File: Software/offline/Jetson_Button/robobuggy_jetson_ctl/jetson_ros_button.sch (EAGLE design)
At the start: 4 parts, among them J1 22-27-2061-06

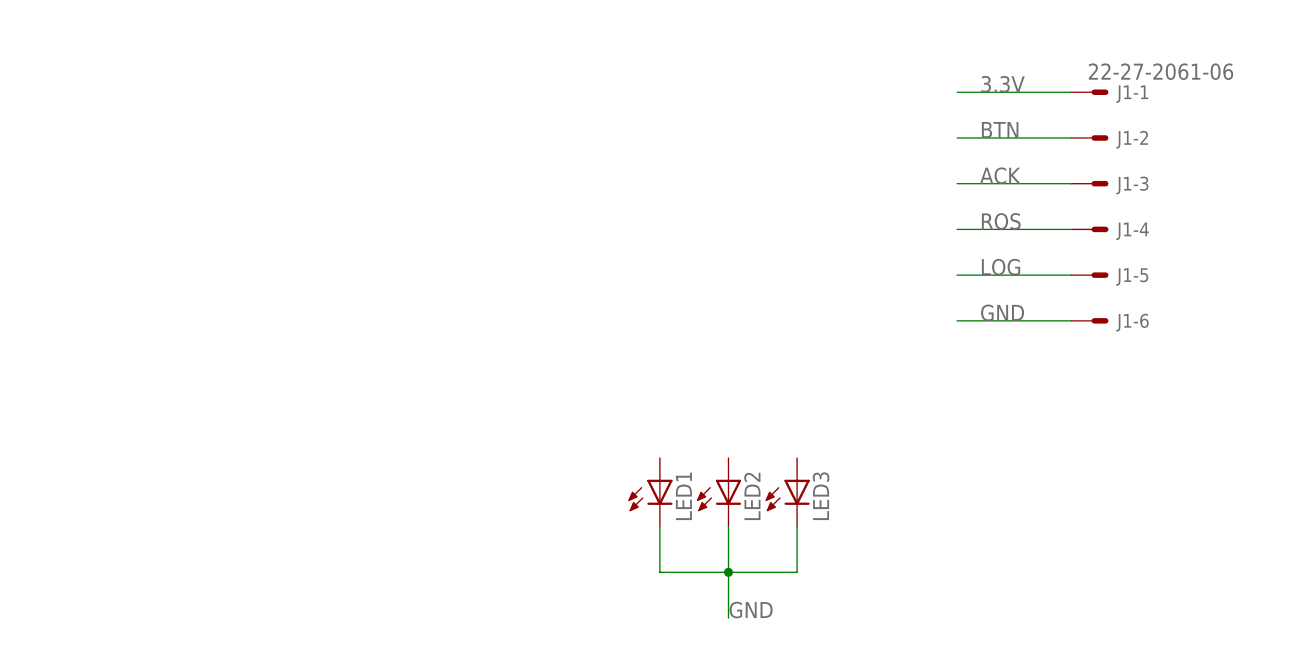
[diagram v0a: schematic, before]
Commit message: Changed connector so that it matches what is on the LED board
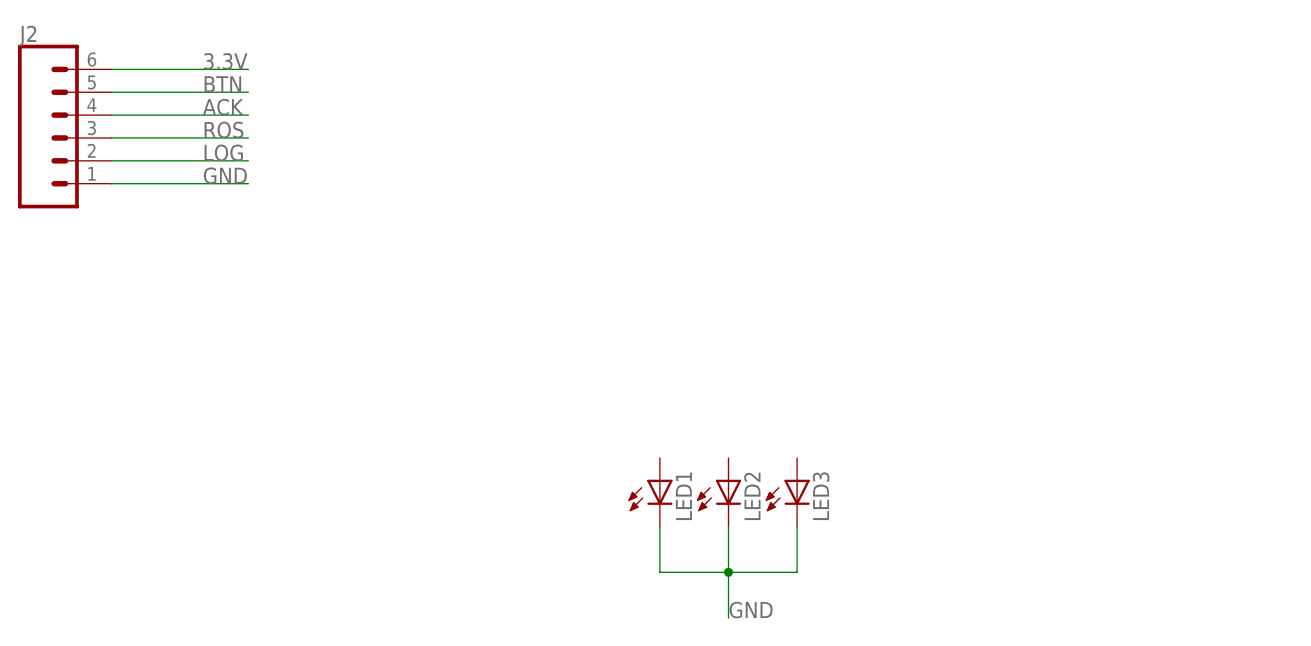
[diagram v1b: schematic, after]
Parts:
- removed J1: 22-27-2061-06, con-molex:22-27-2061-06
- added J2: (no value), SparkFun-Connectors:CONN_06SILK_FEMALE_PTH
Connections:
- net 3.3V: now also J2.6; no longer J1-1.S
- net ACK: now also J2.4; no longer J1-3.S
- net BTN: now also J2.5; no longer J1-2.S
- net GND: now also J2.1; no longer J1-6.S
- net LOG: now also J2.2; no longer J1-5.S
- net ROS: now also J2.3; no longer J1-4.S

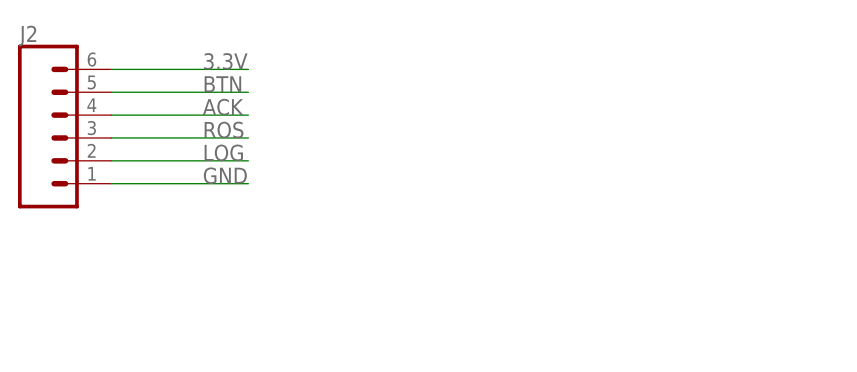
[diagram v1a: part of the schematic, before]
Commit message: Add the push button to the PCB
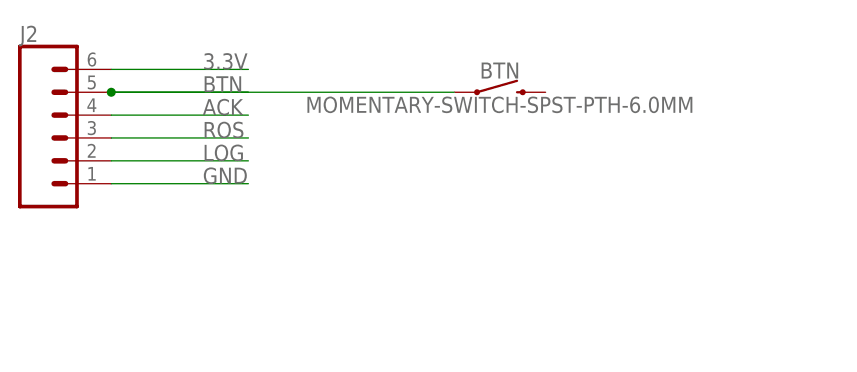
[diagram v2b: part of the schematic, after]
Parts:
- added BTN: MOMENTARY-SWITCH-SPST-PTH-6.0MM, SparkFun-Switches:MOMENTARY-SWITCH-SPST-PTH-6.0MM
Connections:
- net BTN: now also BTN.1
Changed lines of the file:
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@@
 <part name="LED3" library="eagle-ltspice" library_urn="urn:adsk.eagle:library:217" deviceset="LED_E" device="" package3d_urn="urn:adsk.eagle:package:13319/1"/>
 <part name="J2" library="SparkFun-Connectors" library_urn="urn:adsk.eagle:library:513" deviceset="CONN_06" device="SILK_FEMALE_PTH" package3d_urn="urn:adsk.eagle:package:38009/1"/>
+<part name="BTN" library="SparkFun-Switches" library_urn="urn:adsk.eagle:library:535" deviceset="MOMENTARY-SWITCH-SPST" device="-PTH-6.0MM" package3d_urn="urn:adsk.eagle:package:40163/1"/>
 </parts>
 <sheets>
@@
 <instance part="LED3" gate="G$1" x="274.32" y="139.7"/>
 <instance part="J2" gate="G$1" x="193.04" y="177.8"/>
+<instance part="BTN" gate="G$1" x="241.3" y="182.88"/>
 </instances>
 <busses>
@@
 <wire x1="198.12" y1="182.88" x2="213.36" y2="182.88" width="0.1524" layer="91"/>
 <label x="208.28" y="182.88" size="1.778" layer="95"/>
+<pinref part="BTN" gate="G$1" pin="1"/>
+<wire x1="198.12" y1="182.88" x2="236.22" y2="182.88" width="0.1524" layer="91"/>
+<junction x="198.12" y="182.88"/>
 </segment>
 </net>

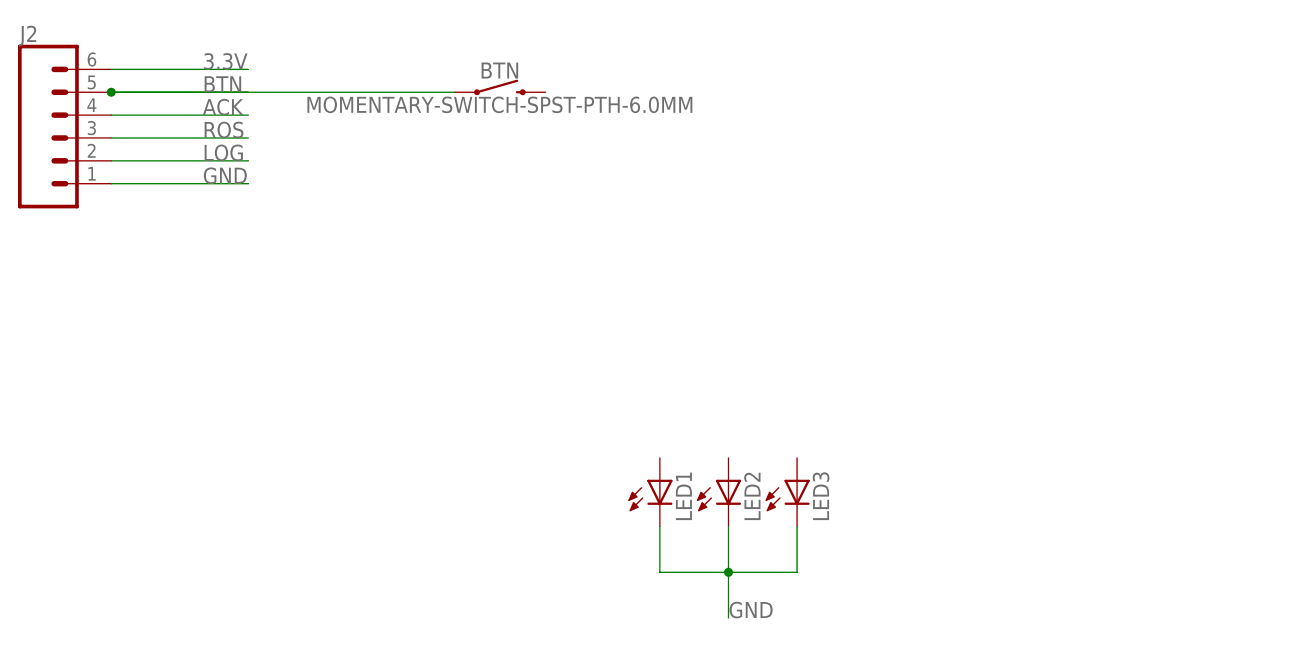
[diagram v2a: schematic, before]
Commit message: Added in resistors and arranged PCB layout
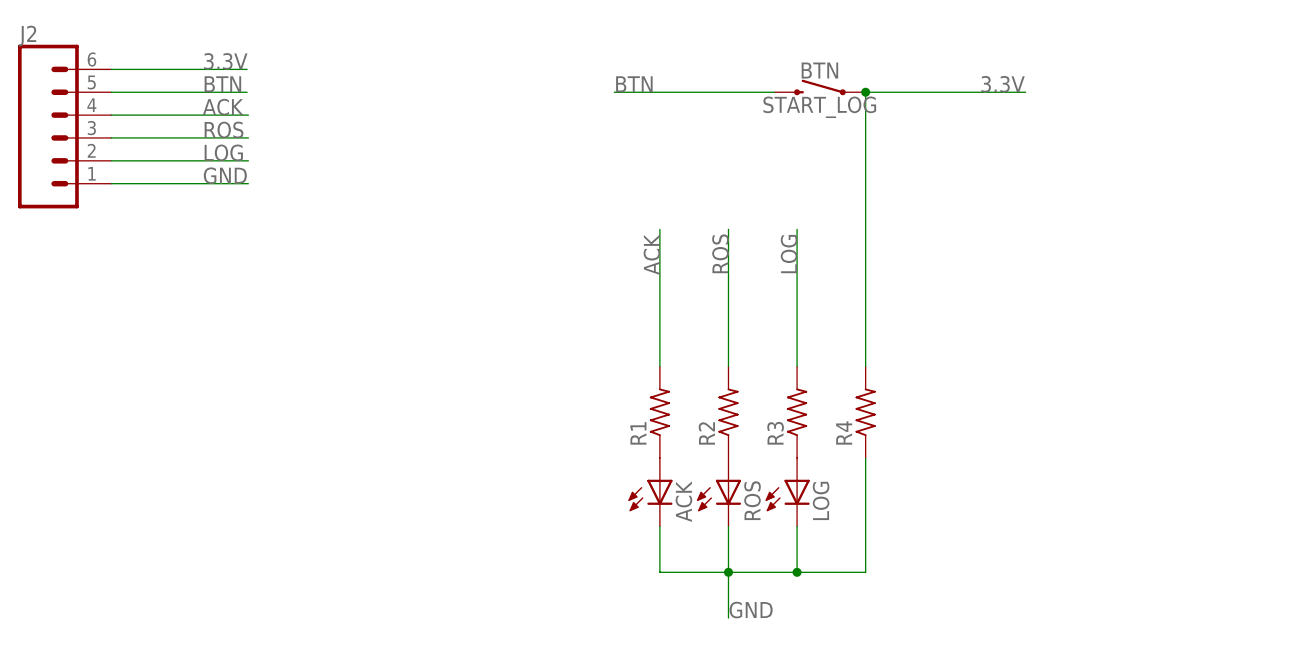
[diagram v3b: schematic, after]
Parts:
- added R1, R2, R3, R4: (no value), rcl:R-US_0204/7
- BTN: value MOMENTARY-SWITCH-SPST-PTH-6.0MM -> START_LOG
- renumbered LED1 to ACK, LED2 to ROS, LED3 to LOG
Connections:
- new net N$1: ACK.A, R1.1
- new net N$2: R2.1, ROS.A
- new net N$3: LOG.A, R3.1
- net 3.3V: now also BTN.1, R4.2
- net ACK: now also R1.2
- net BTN: now also BTN.2; no longer BTN.1
- net GND: now also R4.1
- net LOG: now also R3.2
- net ROS: now also R2.2
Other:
- moved on the sheet: BTN
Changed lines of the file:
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@@
 <parts>
 <part name="FRAME1" library="frames" library_urn="urn:adsk.eagle:library:229" deviceset="A3L-LOC" device=""/>
-<part name="LED1" library="eagle-ltspice" library_urn="urn:adsk.eagle:library:217" deviceset="LED_E" device="" package3d_urn="urn:adsk.eagle:package:13319/1"/>
-<part name="LED2" library="eagle-ltspice" library_urn="urn:adsk.eagle:library:217" deviceset="LED_E" device="" package3d_urn="urn:adsk.eagle:package:13319/1"/>
-<part name="LED3" library="eagle-ltspice" library_urn="urn:adsk.eagle:library:217" deviceset="LED_E" device="" package3d_urn="urn:adsk.eagle:package:13319/1"/>
+<part name="ACK" library="eagle-ltspice" library_urn="urn:adsk.eagle:library:217" deviceset="LED_E" device="" package3d_urn="urn:adsk.eagle:package:13319/1"/>
+<part name="ROS" library="eagle-ltspice" library_urn="urn:adsk.eagle:library:217" deviceset="LED_E" device="" package3d_urn="urn:adsk.eagle:package:13319/1"/>
+<part name="LOG" library="eagle-ltspice" library_urn="urn:adsk.eagle:library:217" deviceset="LED_E" device="" package3d_urn="urn:adsk.eagle:package:13319/1"/>
 <part name="J2" library="SparkFun-Connectors" library_urn="urn:adsk.eagle:library:513" deviceset="CONN_06" device="SILK_FEMALE_PTH" package3d_urn="urn:adsk.eagle:package:38009/1"/>
-<part name="BTN" library="SparkFun-Switches" library_urn="urn:adsk.eagle:library:535" deviceset="MOMENTARY-SWITCH-SPST" device="-PTH-6.0MM" package3d_urn="urn:adsk.eagle:package:40163/1"/>
+<part name="BTN" library="SparkFun-Switches" library_urn="urn:adsk.eagle:library:535" deviceset="MOMENTARY-SWITCH-SPST" device="-PTH-6.0MM" package3d_urn="urn:adsk.eagle:package:40163/1" value="START_LOG"/>
+<part name="R1" library="rcl" library_urn="urn:adsk.eagle:library:334" deviceset="R-US_" device="0204/7" package3d_urn="urn:adsk.eagle:package:23498/1"/>
+<part name="R2" library="rcl" library_urn="urn:adsk.eagle:library:334" deviceset="R-US_" device="0204/7" package3d_urn="urn:adsk.eagle:package:23498/1"/>
+<part name="R3" library="rcl" library_urn="urn:adsk.eagle:library:334" deviceset="R-US_" device="0204/7" package3d_urn="urn:adsk.eagle:package:23498/1"/>
+<part name="R4" library="rcl" library_urn="urn:adsk.eagle:library:334" deviceset="R-US_" device="0204/7" package3d_urn="urn:adsk.eagle:package:23498/1"/>
 </parts>
 <sheets>
@@
 <instances>
 <instance part="FRAME1" gate="G$1" x="-22.86" y="-12.7"/>
-<instance part="LED1" gate="G$1" x="259.08" y="139.7"/>
-<instance part="LED2" gate="G$1" x="266.7" y="139.7"/>
-<instance part="LED3" gate="G$1" x="274.32" y="139.7"/>
+<instance part="ACK" gate="G$1" x="259.08" y="139.7"/>
+<instance part="ROS" gate="G$1" x="266.7" y="139.7"/>
+<instance part="LOG" gate="G$1" x="274.32" y="139.7"/>
 <instance part="J2" gate="G$1" x="193.04" y="177.8"/>
-<instance part="BTN" gate="G$1" x="241.3" y="182.88"/>
+<instance part="BTN" gate="G$1" x="276.86" y="182.88" rot="MR0"/>
+<instance part="R1" gate="G$1" x="259.08" y="147.32" rot="R90"/>
+<instance part="R2" gate="G$1" x="266.7" y="147.32" rot="R90"/>
+<instance part="R3" gate="G$1" x="274.32" y="147.32" rot="R90"/>
+<instance part="R4" gate="G$1" x="281.94" y="147.32" rot="R90"/>
 </instances>
 <busses>
@@
 <net name="GND" class="0">
 <segment>
-<pinref part="LED1" gate="G$1" pin="C"/>
+<pinref part="ACK" gate="G$1" pin="C"/>
 <wire x1="259.08" y1="134.62" x2="259.08" y2="129.54" width="0.1524" layer="91"/>
 <wire x1="259.08" y1="129.54" x2="266.7" y2="129.54" width="0.1524" layer="91"/>
-<pinref part="LED3" gate="G$1" pin="C"/>
+<pinref part="LOG" gate="G$1" pin="C"/>
 <wire x1="266.7" y1="129.54" x2="274.32" y2="129.54" width="0.1524" layer="91"/>
 <wire x1="274.32" y1="129.54" x2="274.32" y2="134.62" width="0.1524" layer="91"/>
-<pinref part="LED2" gate="G$1" pin="C"/>
+<pinref part="ROS" gate="G$1" pin="C"/>
 <wire x1="266.7" y1="134.62" x2="266.7" y2="129.54" width="0.1524" layer="91"/>
 <junction x="266.7" y="129.54"/>
 <wire x1="266.7" y1="129.54" x2="266.7" y2="124.46" width="0.1524" layer="91"/>
 <label x="266.7" y="124.46" size="1.778" layer="95"/>
+<pinref part="R4" gate="G$1" pin="1"/>
+<wire x1="281.94" y1="142.24" x2="281.94" y2="129.54" width="0.1524" layer="91"/>
+<wire x1="281.94" y1="129.54" x2="274.32" y2="129.54" width="0.1524" layer="91"/>
+<junction x="274.32" y="129.54"/>
 </segment>
 <segment>
@@
 <net name="3.3V" class="0">
 <segment>
+<pinref part="R4" gate="G$1" pin="2"/>
+<pinref part="BTN" gate="G$1" pin="1"/>
+<wire x1="281.94" y1="182.88" x2="281.94" y2="152.4" width="0.1524" layer="91"/>
+<wire x1="299.72" y1="182.88" x2="281.94" y2="182.88" width="0.1524" layer="91"/>
+<junction x="281.94" y="182.88"/>
+<label x="294.64" y="182.88" size="1.778" layer="95"/>
+</segment>
+<segment>
 <pinref part="J2" gate="G$1" pin="6"/>
-<wire x1="198.12" y1="185.42" x2="213.36" y2="185.42" width="0.1524" layer="91"/>
+<wire x1="213.2076" y1="185.42" x2="198.12" y2="185.42" width="0.1524" layer="91"/>
 <label x="208.28" y="185.42" size="1.778" layer="95"/>
 </segment>
@@
 <net name="BTN" class="0">
 <segment>
+<pinref part="BTN" gate="G$1" pin="2"/>
+<wire x1="254" y1="182.88" x2="271.78" y2="182.88" width="0.1524" layer="91"/>
+<label x="254" y="182.88" size="1.778" layer="95"/>
+</segment>
+<segment>
 <pinref part="J2" gate="G$1" pin="5"/>
-<wire x1="198.12" y1="182.88" x2="213.36" y2="182.88" width="0.1524" layer="91"/>
+<wire x1="213.2076" y1="182.88" x2="198.12" y2="182.88" width="0.1524" layer="91"/>
 <label x="208.28" y="182.88" size="1.778" layer="95"/>
-<pinref part="BTN" gate="G$1" pin="1"/>
-<wire x1="198.12" y1="182.88" x2="236.22" y2="182.88" width="0.1524" layer="91"/>
-<junction x="198.12" y="182.88"/>
 </segment>
 </net>
@@
 <label x="208.28" y="180.34" size="1.778" layer="95"/>
 </segment>
+<segment>
+<pinref part="R1" gate="G$1" pin="2"/>
+<wire x1="259.08" y1="152.4" x2="259.08" y2="167.64" width="0.1524" layer="91"/>
+<label x="259.08" y="162.56" size="1.778" layer="95" rot="R90"/>
+</segment>
 </net>
 <net name="ROS" class="0">
@@
 <label x="208.28" y="177.8" size="1.778" layer="95"/>
 </segment>
+<segment>
+<pinref part="R2" gate="G$1" pin="2"/>
+<wire x1="266.7" y1="152.4" x2="266.7" y2="167.64" width="0.1524" layer="91"/>
+<label x="266.7" y="162.56" size="1.778" layer="95" rot="R90"/>
+</segment>
 </net>
 <net name="LOG" class="0">
@@
 <wire x1="198.12" y1="175.26" x2="213.36" y2="175.26" width="0.1524" layer="91"/>
 <label x="208.28" y="175.26" size="1.778" layer="95"/>
+</segment>
+<segment>
+<pinref part="R3" gate="G$1" pin="2"/>
+<wire x1="274.32" y1="152.4" x2="274.32" y2="167.64" width="0.1524" layer="91"/>
+<label x="274.32" y="162.56" size="1.778" layer="95" rot="R90"/>
+</segment>
+</net>
+<net name="N$1" class="0">
+<segment>
+<pinref part="ACK" gate="G$1" pin="A"/>
+<pinref part="R1" gate="G$1" pin="1"/>
+</segment>
+</net>
+<net name="N$2" class="0">
+<segment>
+<pinref part="ROS" gate="G$1" pin="A"/>
+<pinref part="R2" gate="G$1" pin="1"/>
+</segment>
+</net>
+<net name="N$3" class="0">
+<segment>
+<pinref part="LOG" gate="G$1" pin="A"/>
+<pinref part="R3" gate="G$1" pin="1"/>
 </segment>
 </net>
@@
 packages will not be understood (or retained) with this version.
 </note>
+<note version="8.4" severity="warning">
+Since Version 8.4, EAGLE supports properties for SPICE simulation.
+Probes in schematics and SPICE mapping objects found in parts and library devices
+will not be understood with this version. Update EAGLE to the latest version
+for full support of SPICE simulation.
+</note>
 </compatibility>
